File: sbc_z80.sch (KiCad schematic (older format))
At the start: 9 parts, among them J1 Conn_02x40_Top_Bottom, U1 Z84C4310AEG, U3 IS62C5128BL-45TLI, U4 27C512PLCC, U6 Z84C0010AEG, U7 EPM7032STC44, U8 Z84C3010AEG, U9 Z84C2010AEG

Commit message: added 3V3 section for clock generator
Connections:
- wire segments 195 -> 209
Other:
- note added: "SRAM"

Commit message: larger sheet, connected more pins
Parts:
- removed RN1: 10K, Resistor_SMD:R_Array_Concave_4x0603, symbol Device:R_Pack04
- removed U1: Z84C4310AEG, Package_QFP:LQFP-44_10x10mm_P0.8mm, symbol zilog:Z84C4310AEG
- removed U4: 27C512PLCC, Package_LCC:PLCC-32_11.4x14.0mm_P1.27mm, symbol Memory_EPROM:27C512PLCC
- removed U6: Z84C0010AEG, Package_QFP:LQFP-44_10x10mm_P0.8mm, symbol zilog:Z84C0010AEG
- added C10, C11, C12, C13, C14, C5, C6, C7, C8, C9: 100nF, Capacitor_SMD:C_0603_1608Metric_Pad1.05x0.95mm_HandSolder, symbol Device:C_Small
- added J3: Conn_02x12_Odd_Even, symbol Connector_Generic:Conn_02x12_Odd_Even
- added R4, R5, R6, R7, R8: 10K, Resistor_SMD:R_0603_1608Metric_Pad1.05x0.95mm_HandSolder, symbol Device:R_Small
- added U1: CPU - Z84C0010AEG, Package_QFP:LQFP-44_10x10mm_P0.8mm, symbol zilog:Z84C0010AEG
- added U4: ROM - GLS29EE512, Package_LCC:PLCC-32_11.4x14.0mm_P1.27mm, symbol Memory_EEPROM:GLS29EE512
- added U6: SIO/3 - Z84C4310AEG, Package_QFP:LQFP-44_10x10mm_P0.8mm, symbol zilog:Z84C4310AEG
- J1: value Conn_02x40_Top_Bottom -> RC80 Bus
- U3: value IS62C5128BL-45TLI -> SRAM - IS62C5128BL-45TLI; symbol Memory_RAM:IS62C5128BL-45TLI -> sbc_z80-rescue:IS62C5128BL-45TLI-Memory_RAM
- U7: value EPM7032STC44 -> CPLD - EPM7032STC44; symbol CPLD_Altera:EPM7032STC44 -> sbc_z80-rescue:EPM7032STC44-CPLD_Altera
- U8: value Z84C3010AEG -> CTC - Z84C3010AEG
- U9: value Z84C2010AEG -> PIO - Z84C2010AEG
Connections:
- net labels added: +5V, CLK2, CLK_F, CLK_U, RAM_CE, ~BUSREQ, ~CE, ~OE
- net labels removed: 5V, ~BUSRQ, ~CLK2
- wire segments 209 -> 286
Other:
- moved on the sheet: J1

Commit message: started routing
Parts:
- added J4, J5: Conn_01x06, Connector_PinHeader_2.54mm:PinHeader_1x06_P2.54mm_Horizontal, symbol Connector_Generic:Conn_01x06
- J3: footprint (none) -> Connector_PinHeader_2.54mm:PinHeader_2x12_P2.54mm_Horizontal
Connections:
- net labels added: PAGE, ROM_CE
- wire segments 286 -> 300
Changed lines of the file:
@@
 F 0 "J3" H 13830 5942 50  0000 C CNN
 F 1 "Conn_02x12_Odd_Even" H 13830 5851 50  0000 C CNN
-F 2 "" H 13780 5225 50  0001 C CNN
+F 2 "Connector_PinHeader_2.54mm:PinHeader_2x12_P2.54mm_Horizontal" H 13780 5225 50  0001 C CNN
 F 3 "~" H 13780 5225 50  0001 C CNN
 	1    13780 5225
@@
 	0    1    1    0
 $EndComp
+Text Label 7735 2505 2    50   ~ 0
+~NMI
+Text Label 7735 2255 2    50   ~ 0
+~WAIT
+Text Label 7735 2155 2    50   ~ 0
+~HALT
+Text Label 7735 1605 2    50   ~ 0
+~WR
+Text Label 7735 1505 2    50   ~ 0
+~RD
+Text Label 7735 1255 2    50   ~ 0
+PAGE
+Text Label 7775 1155 2    50   ~ 0
+ROM_CE
+Entry Wire Line
+	7905 2405 7805 2505
+Entry Wire Line
+	7905 1705 7805 1805
+Entry Wire Line
+	7905 2055 7805 2155
+Entry Wire Line
+	7905 1505 7805 1605
+Entry Wire Line
+	7905 1405 7805 1505
+Entry Wire Line
+	7905 1155 7805 1255
+Entry Wire Line
+	7905 1055 7805 1155
+Entry Wire Line
+	7905 955  7805 1055
+Wire Wire Line
+	7545 2505 7805 2505
+Wire Wire Line
+	7545 1805 7805 1805
+Wire Wire Line
+	7545 2155 7805 2155
+Wire Wire Line
+	7545 1605 7805 1605
+Wire Wire Line
+	7545 1505 7805 1505
+Wire Wire Line
+	7545 1255 7805 1255
+Wire Wire Line
+	7545 1155 7805 1155
+Wire Wire Line
+	7545 1055 7805 1055
+Entry Wire Line
+	7805 3405 7905 3305
+Text Label 7735 3405 2    50   ~ 0
+CLK
+Wire Wire Line
+	7545 3405 7805 3405
+Entry Wire Line
+	7905 2155 7805 2255
+Wire Wire Line
+	7545 2255 7805 2255
+Entry Wire Line
+	7905 2505 7805 2605
+Wire Wire Line
+	7545 2605 7805 2605
+Entry Wire Line
+	7905 2655 7805 2755
+Wire Wire Line
+	7545 2755 7805 2755
+Entry Wire Line
+	7905 2905 7805 3005
+Wire Wire Line
+	7545 3005 7805 3005
+Entry Wire Line
+	7905 3005 7805 3105
+Wire Wire Line
+	7545 3105 7805 3105
+Text Label 7800 1055 2    50   ~ 0
+RAM_CE
+Text Label 7730 2605 2    50   ~ 0
+~INT
+Text Label 7770 2755 2    50   ~ 0
+~RESET
+Text Label 7780 3005 2    50   ~ 0
+~BUSREQ
+Text Label 7775 3105 2    50   ~ 0
+~BUSACK
 Wire Bus Line
 	7060 6225 7060 6610
@@
 	4740 935  4740 3385
 Wire Bus Line
+	7905 910  7905 3360
+Wire Bus Line
 	4835 4435 4835 6315
 Wire Bus Line
@@
 Wire Bus Line
 	9885 885  9885 6255
+$Comp
+L Connector_Generic:Conn_01x06 J4
+U 1 1 5D23E8B7
+P 13230 1350
+F 0 "J4" H 13310 1342 50  0000 L CNN
+F 1 "Conn_01x06" H 13310 1251 50  0000 L CNN
+F 2 "Connector_PinHeader_2.54mm:PinHeader_1x06_P2.54mm_Horizontal" H 13230 1350 50  0001 C CNN
+F 3 "~" H 13230 1350 50  0001 C CNN
+	1    13230 1350
+	1    0    0    -1
+$EndComp
+$Comp
+L Connector_Generic:Conn_01x06 J5
+U 1 1 5D23FD21
+P 13210 2170
+F 0 "J5" H 13290 2162 50  0000 L CNN
+F 1 "Conn_01x06" H 13290 2071 50  0000 L CNN
+F 2 "Connector_PinHeader_2.54mm:PinHeader_1x06_P2.54mm_Horizontal" H 13210 2170 50  0001 C CNN
+F 3 "~" H 13210 2170 50  0001 C CNN
+	1    13210 2170
+	1    0    0    -1
+$EndComp
 $EndSCHEMATC

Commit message: fixed up ce signals
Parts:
- added J6: Conn_01x10, Connector_PinHeader_2.54mm:PinHeader_1x10_P2.54mm_Horizontal, symbol Connector_Generic:Conn_01x10
- added R10, R11, R12, R13, R16, R17, R18, R19: 2.2K, Resistor_SMD:R_0603_1608Metric_Pad1.05x0.95mm_HandSolder, symbol Device:R_Small
- added R14, R15, R20, R9: 100K, Resistor_SMD:R_0603_1608Metric_Pad1.05x0.95mm_HandSolder, symbol Device:R_Small
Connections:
- net labels added: CTC_CE, PIO_CE, SIO_CE, ~BANK, ~CTSA, ~CTSB, ~IORD, ~IOWR, ~MEMRD, ~MEMWR, ~RTSA, ~RTSB, ~RXCA, ~TXCA
- net labels removed: RAM_CE, ROM_CE, ~CE, ~OE
- wire segments 300 -> 335
- no-connect marks 8 -> 18
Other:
- moved on the sheet: J4, R4

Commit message: reordered resistors
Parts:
- added J7: AVR-JTAG-10, Connector_PinHeader_1.27mm:PinHeader_2x05_P1.27mm_Vertical, symbol Connector:AVR-JTAG-10
- added R21: 1K, Resistor_SMD:R_0603_1608Metric_Pad1.05x0.95mm_HandSolder, symbol Device:R_Small
- added R22, R23, R24: 10K, Resistor_SMD:R_0603_1608Metric_Pad1.05x0.95mm_HandSolder, symbol Device:R_Small
- added SW1: SW_Push, Button_Switch_SMD:SW_SPST_FSMSM, symbol Switch:SW_Push
- added U12: MIC811LUY, Package_TO_SOT_SMD:SOT-143, symbol Power_Supervisor:MIC811LUY
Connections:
- net labels added: BANK1, BANK2, BANK3, TCK, TDI, TDO, TMS
- net labels removed: ~BANK, ~RXCA, ~TXCA
- wire segments 335 -> 373
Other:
- moved on the sheet: C10, C11, C12, C13, C14, C5, C6, C7, C8, C9, U7

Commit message: changed part layouts
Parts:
- removed U4: ROM - GLS29EE512, Package_LCC:PLCC-32_11.4x14.0mm_P1.27mm, symbol Memory_EEPROM:GLS29EE512
- added R25, R26, R27, R28: 10K, Resistor_SMD:R_0603_1608Metric_Pad1.05x0.95mm_HandSolder, symbol Device:R_Small
- added U4: GLS29EE010, Package_LCC:PLCC-32_SMD-Socket, symbol sbc_z80-rescue:GLS29EE010
- J3: value Conn_02x12_Odd_Even -> PIO Header; footprint Connector_PinHeader_2.54mm:PinHeader_2x12_P2.54mm_Horizontal -> Connector_PinHeader_2.54mm:PinHeader_2x13_P2.54mm_Horizontal; symbol Connector_Generic:Conn_02x12_Odd_Even -> Connector_Generic:Conn_02x13_Odd_Even
- J6: value Conn_01x10 -> CTC Header
- R10, R11, R12, R13, R16, R17, R18, R19: value 2.2K -> 2K2
- U1: symbol zilog:Z84C0010AEG -> sbc_z80-rescue:Z84C0010AEG-zilog
- U6: symbol zilog:Z84C4310AEG -> sbc_z80-rescue:Z84C4310AEG-zilog
- U8: symbol zilog:Z84C3010AEG -> sbc_z80-rescue:Z84C3010AEG-zilog
- U9: symbol zilog:Z84C2010AEG -> sbc_z80-rescue:Z84C2010AEG-zilog
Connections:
- net labels added: ARDY, BRDY, CLKX, CT0, CT1, CT2, CT3, PA0, PA1, PA2, PA3, PA4, PA5, PA6, PA7, PB0, PB1, PB2, PB3, PB4, PB5, PB6, PB7, ZT0, ZT1, ZT2, ~ASTB, ~BSTB
- net labels removed: BANK1, BANK2, BANK3
- wire segments 373 -> 458
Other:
- note added: "EEPROM 128Kx8"
- note added: "SRAM 512Kx8"
- note removed: "SRAM"
- moved on the sheet: J4, J5, J6, R10, R11, R12, R13, R14, R15, R16, R17, R18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

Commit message: cleanup
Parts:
- added D1: Red/Green, LED_SMD:LED_2C_0603_1608Metric_Pad1.05x0.95mm_HandSolder, symbol Device:LED_Dual_ACAC
- added R29, R30: 680R, Resistor_SMD:R_0603_1608Metric_Pad1.05x0.95mm_HandSolder, symbol Device:R_Small
- added SW3: SW_DIP_x08, Button_Switch_SMD:SW_DIP_SPSTx08_Slide_KingTek_DSHP08TJ_W5.25mm_P1.27mm_JPin, symbol Switch:SW_DIP_x08
- added U10: 74HC04, symbol 74xx:74HC04
- U7: footprint Package_QFP:TQFP-44_10x10mm_P0.8mm -> Package_QFP:TQFP-100_14x14mm_P0.5mm
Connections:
- net +5V: now also R29.2, R30.2
- net PAGE: now also U10.11
- new net: D1.1 (A1), R29.1
- new net: D1.2 (K1), U10.10, U10.9
- new net: D1.3 (A2), R30.1
- new net: D1.4 (K2), U10.8
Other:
- moved on the sheet: J7, R21, R22, R23, R24

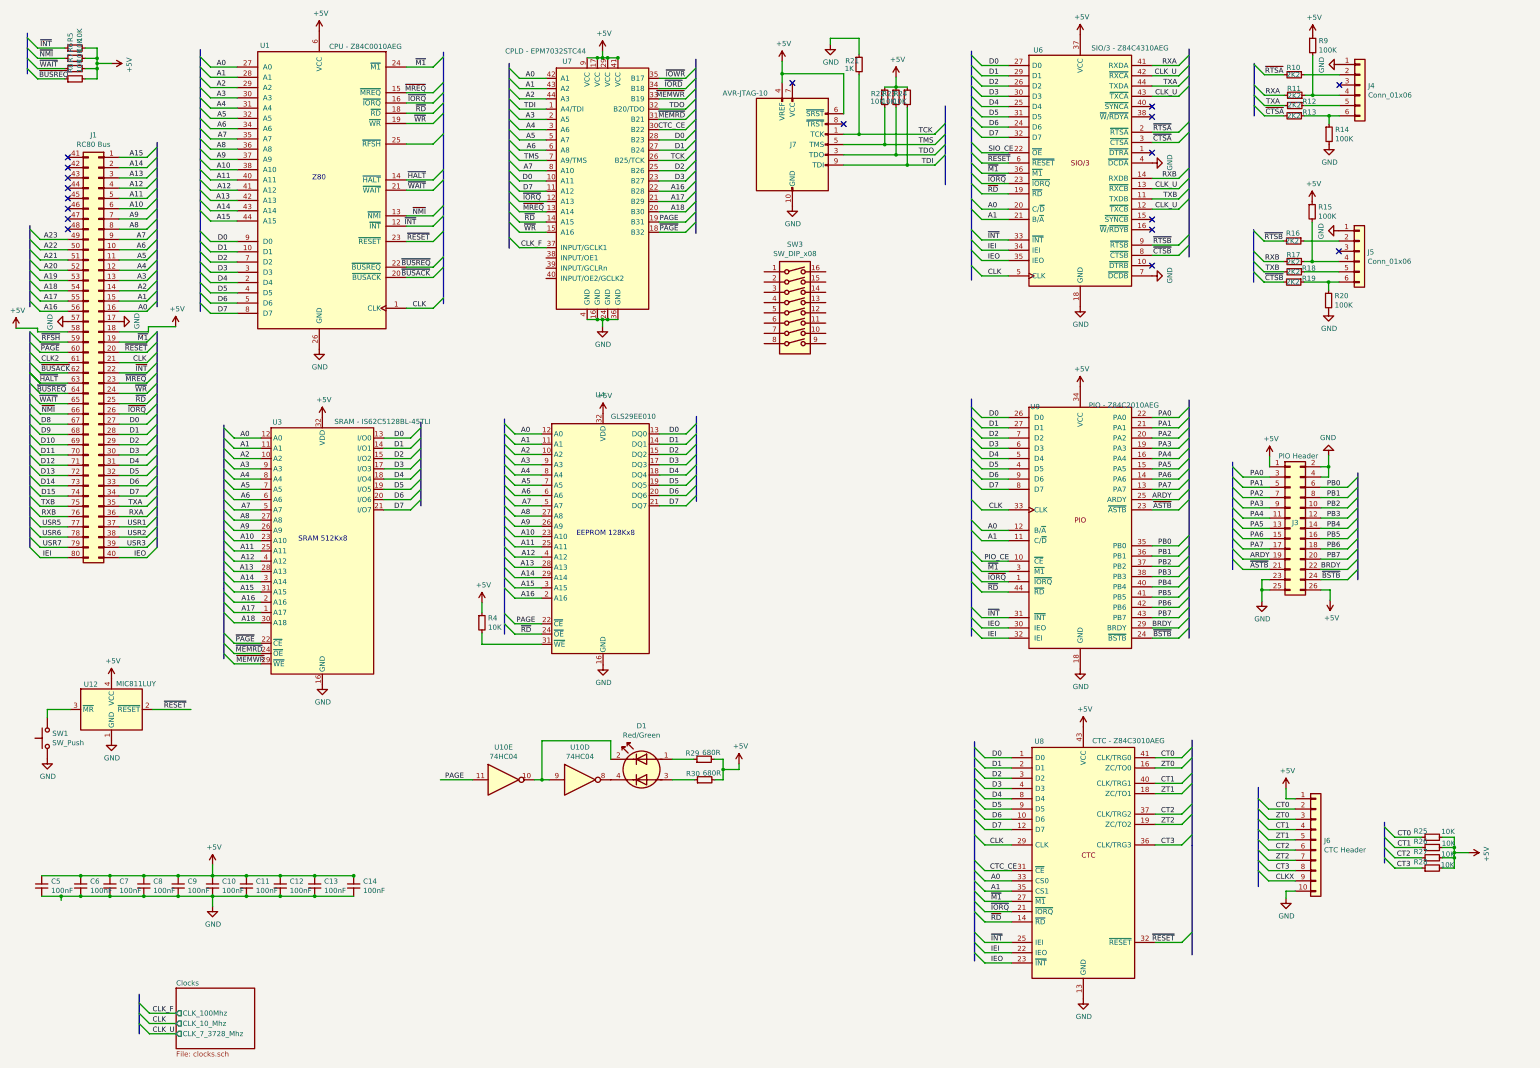
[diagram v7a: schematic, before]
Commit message: added display, config switch
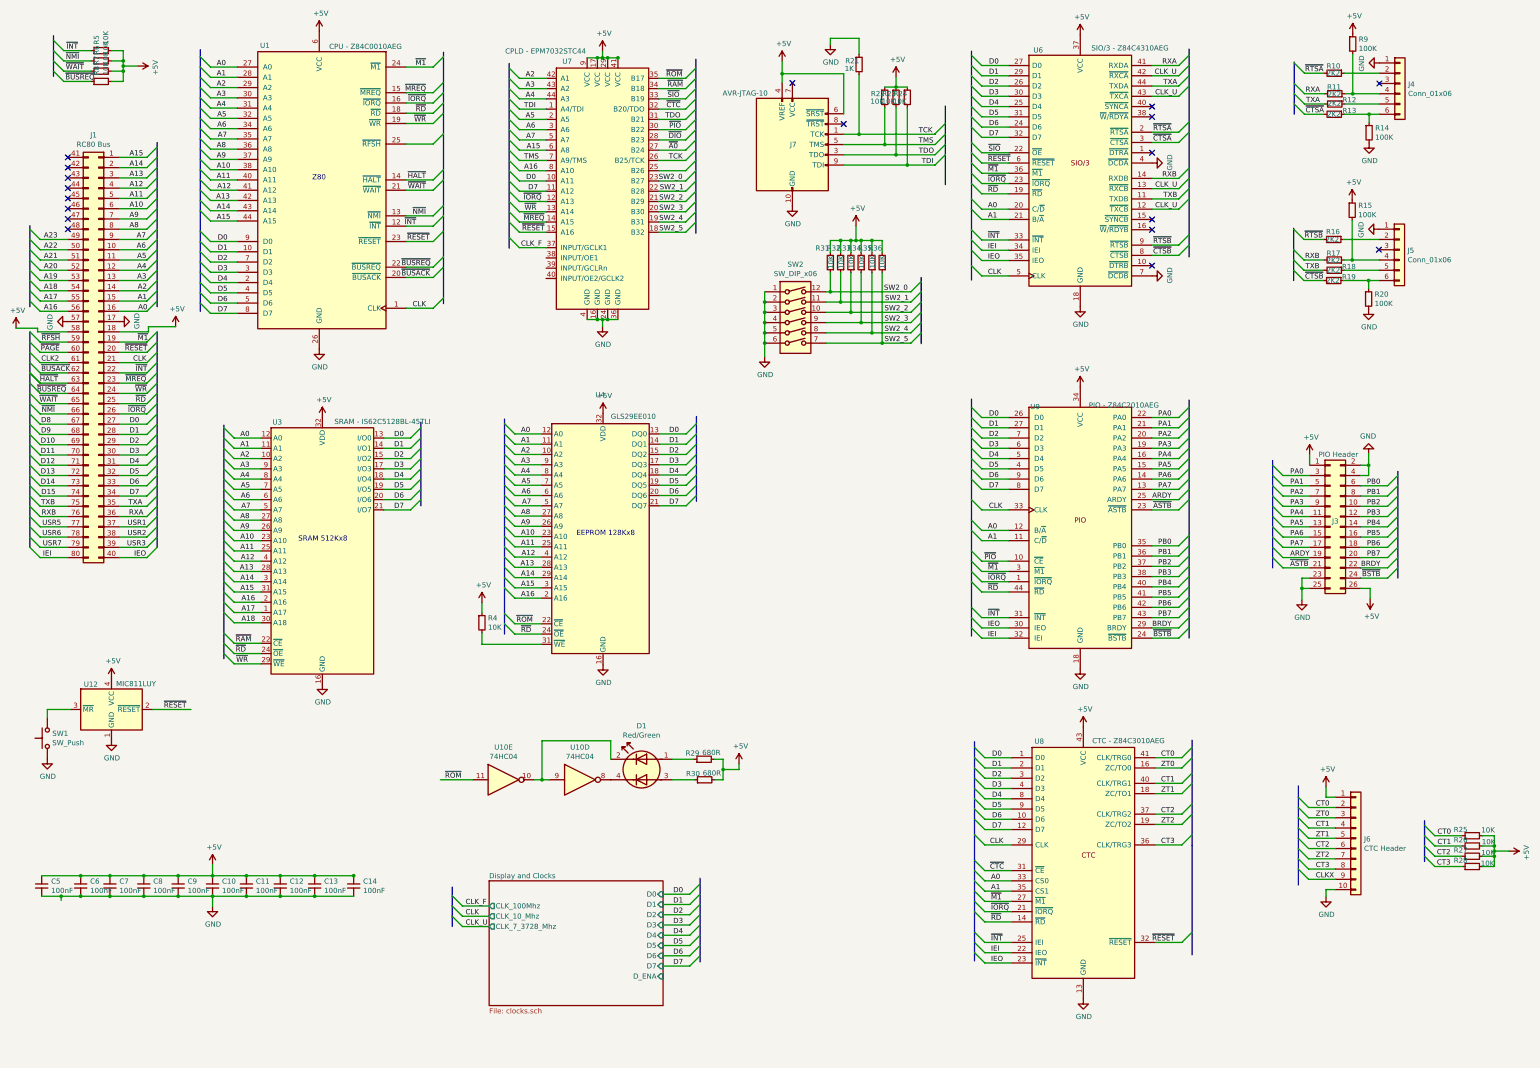
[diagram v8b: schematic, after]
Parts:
- removed SW3: SW_DIP_x08, Button_Switch_SMD:SW_DIP_SPSTx08_Slide_KingTek_DSHP08TJ_W5.25mm_P1.27mm_JPin, symbol Switch:SW_DIP_x08
- added R31, R32, R33, R34, R35, R36: 10K, Resistor_SMD:R_0603_1608Metric_Pad1.05x0.95mm_HandSolder, symbol Device:R_Small
- added SW2: SW_DIP_x06, Button_Switch_SMD:SW_DIP_SPSTx06_Slide_Copal_CHS-06A_W5.08mm_P1.27mm_JPin, symbol Switch:SW_DIP_x06
- U7: footprint Package_QFP:TQFP-100_14x14mm_P0.5mm -> Package_QFP:TQFP-44_10x10mm_P0.8mm
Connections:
- net ~IOWR is gone; now on net ~ROM: U7.35 (B17)
- net +5V: now also R31.2, R32.2, R33.2, R34.2, R35.2, R36.2
- net A0: no longer U7.42 (A1)
- net A1: no longer U7.43 (A2)
- net A15: now also U7.6 (A8)
- net A16: now also U7.8 (A10); no longer U7.22 (B28)
- net A17: no longer U7.21 (B29)
- net A18: no longer U7.20 (B30)
- net A2: now also U7.42 (A1); no longer U7.44 (A3)
- net A3: now also U7.43 (A2); no longer U7.2 (A5)
- net A4: now also U7.44 (A3); no longer U7.3 (A6)
- net A5: now also U7.2 (A5); no longer U7.5 (A7)
- net A6: now also U7.3 (A6); no longer U7.6 (A8)
- net A7: now also U7.5 (A7); no longer U7.8 (A10)
- net D0: no longer U7.28 (B23)
- net D1: no longer U7.27 (B24)
- net D2: no longer U7.25 (B26)
- net D3: no longer U7.23 (B27)
- net GND: now also SW2.1, SW2.2, SW2.3, SW2.4, SW2.5, SW2.6
- net TDO: now also U7.31 (B21); no longer U7.32 (B20/TDO)
- net ~MREQ: now also U7.14 (A15); no longer U7.13 (A14)
- net ~PAGE: no longer U3.22 (~CE), U7.18 (B32)
- net ~RD: now also U3.24 (~OE); no longer U7.14 (A15)
- net ~RESET: now also U7.15 (A16)
- net ~WR: now also U3.29 (~WE), U7.13 (A14); no longer U7.15 (A16)
- net CTC_CE renamed ~CTC
- net ~CTC: now also U7.32 (B20/TDO); no longer U7.30 (B22)
- net PAGE renamed ~ROM
- net ~ROM: no longer U7.19 (B31)
- net PIO_CE renamed ~PIO
- net ~PIO: now also U7.30 (B22)
- net SIO_CE renamed ~SIO
- net ~SIO: now also U7.33 (B19)
- net ~IORD renamed ~RAM
- net ~RAM: now also U3.22 (~CE)
- removed net ~MEMRD: U3.24 (~OE), U7.31 (B21)
- removed net ~MEMWR: U3.29 (~WE), U7.33 (B19)
- new net SW2_0: R31.1, SW2.12, U7.23 (B27)
- new net SW2_1: R32.1, SW2.11, U7.22 (B28)
- new net SW2_2: R33.1, SW2.10, U7.21 (B29)
- new net SW2_3: R34.1, SW2.9, U7.20 (B30)
- new net SW2_4: R35.1, SW2.8, U7.19 (B31)
- new net SW2_5: R36.1, SW2.7, U7.18 (B32)
- new net ~A0: U7.27 (B24)
- new net ~DIO: U7.28 (B23)
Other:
- moved on the sheet: J3, J4, J5, J6, R10, R11, R12, R13, R14, R15, R16, R17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
